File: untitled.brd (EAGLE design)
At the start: 54 x 54 mm, 22 parts, among them J3 CORTEX_DEBUG_PTH, J6 USB-MICROB, U1 ATSAMD21G-M, U2 MIC5501-3.0YM5-TR, U3 TPD2S017

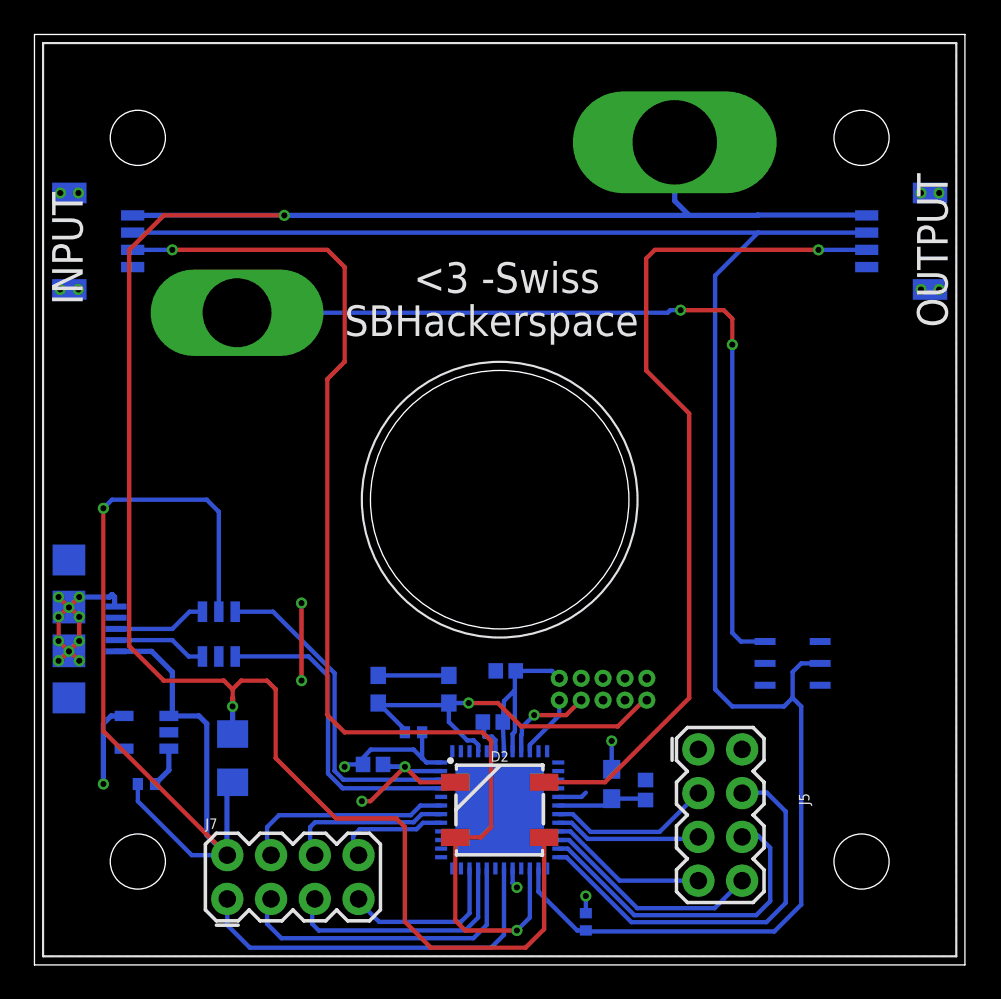
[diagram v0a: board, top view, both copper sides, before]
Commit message: Updated Routing
Updated routing to remove vias. Changed switch wiring to reflect ds2413 example circuit.
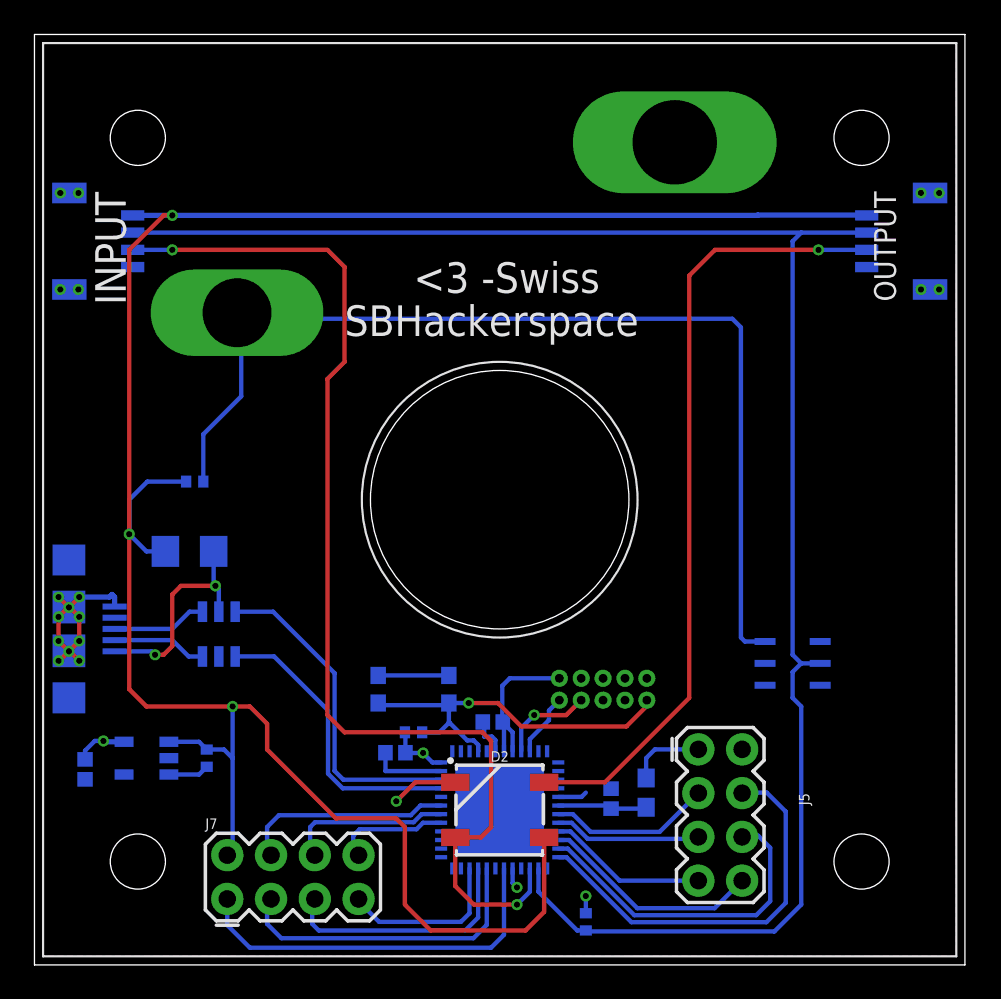
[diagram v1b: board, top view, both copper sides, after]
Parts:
- added R4: 10k, rcl:R0402
- moved C2 25.1 mm to (2.94, 11.3), turned to 270 degrees
- moved F1 12.3 mm to (9.00, 24.0), turned to 180 degrees
- moved R3 3.81 mm to (10.0, 12.0), turned to 90 degrees
- moved C3 2.06 mm to (33.5, 9.65)
- moved FB1 2.06 mm to (35.5, 10.0)
- moved U2 1.50 mm to (6.50, 12.0)
- moved C6 1.47 mm to (20.9, 12.3), turned to 0 degrees
- turned R1 to 0 degrees
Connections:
- net 5V: now also J7.2, R3.2, R4.1, U2.1; no longer U$1.P$3
- net GND: now also U$1.P$3
- net N$10: now also R4.2
- net VBUS: no longer J7.2, R3.2, U2.1
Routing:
- net VBUS: track 64.9 -> 13.0 mm, vias 1 -> 2
- net N$10: track 49.3 -> 59.9 mm, vias 2 -> 0
- net GND: track 58.5 -> 50.7 mm, vias 14 -> 11
- net 1W: track 109.0 -> 101.7 mm
- net VCC: track 28.2 -> 22.4 mm, vias 5 -> 4
- net 5V: track 125.7 -> 130.7 mm, vias 2 -> 3
- net DO: track 50.0 -> 45.9 mm
- net DIO: track 69.1 -> 65.8 mm
- net DO-: track 18.4 -> 17.3 mm

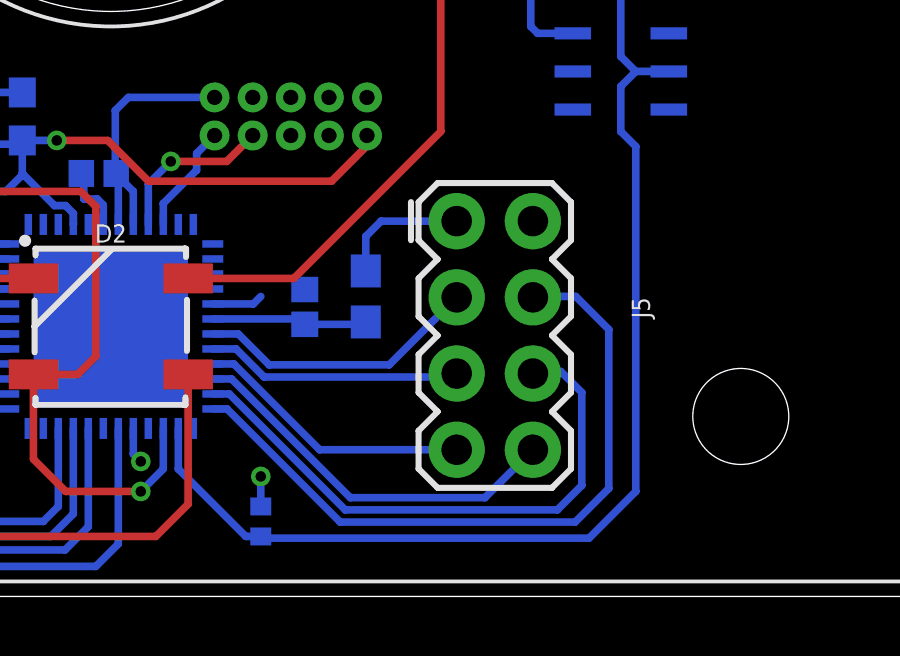
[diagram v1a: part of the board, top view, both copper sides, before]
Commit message: added crystal
added a 32khz crystal per the arduino zero spec. updated routing to fit the crystal and caps.
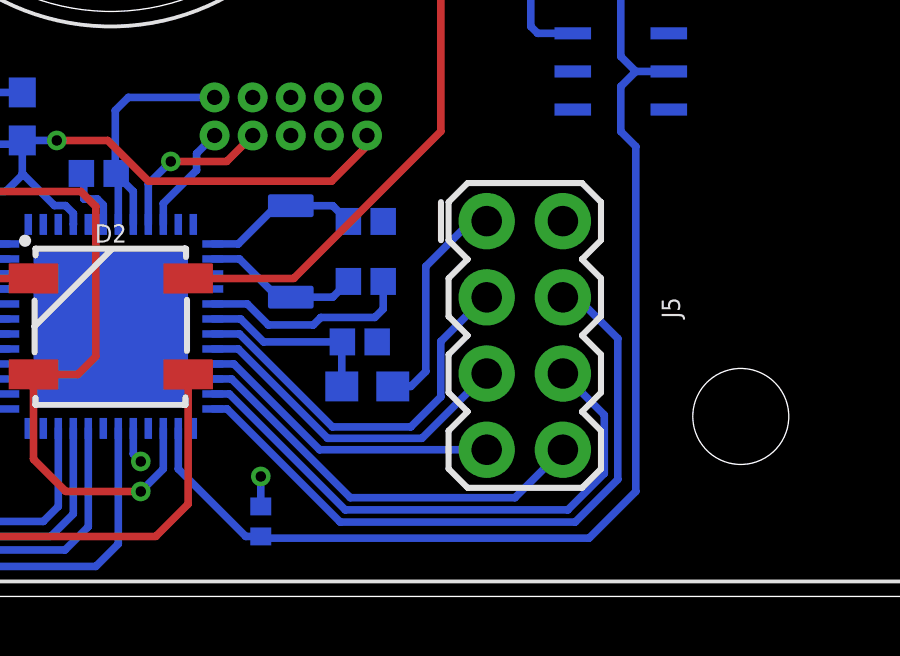
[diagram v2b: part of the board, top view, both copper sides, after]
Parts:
- added C4, C5: 7pf, SparkFun-Capacitors:0402
- added Y1: 32.768KHZ, Seeed-Crystal Oscillator:X2-SMD-3.2X1.5X0.55MM
- moved FB1 3.00 mm to (35.5, 7.00), turned to 0 degrees
- moved C3 2.17 mm to (35.3, 8.48), turned to 180 degrees
- moved J5 1.00 mm to (40.8, 8.70)
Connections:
- new net N$12: C5.2, U1.2, Y1.1
- new net N$13: C4.2, U1.1, Y1.2
- net GND: now also C4.1, C5.1
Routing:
- net GND: track 50.7 -> 56.1 mm
- net N$12: track 0.00 -> 5.28 mm
- net N$13: track 0.00 -> 5.26 mm
- net PA08: track 9.49 -> 13.3 mm
- net VCC: track 22.4 -> 25.5 mm
- net PA09: track 8.57 -> 11.3 mm
- net PA05: track 13.0 -> 14.0 mm
- net PA04: track 9.31 -> 10.3 mm
- net PA07: track 23.5 -> 22.8 mm
- net N$4: track 5.41 -> 6.13 mm
